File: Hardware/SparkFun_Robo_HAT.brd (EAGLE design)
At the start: 65.1 x 57 mm, 235 parts, among them J11 EXT MTR PWR, J18 ISP, J2 RASPBERRYPI-40-PIN-GPIO_SMD_S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, J20 USB C, J23 CORTEX_JTAG_DEBUG_PTH, J7 EXT SERVO PWR, J8 EXT 5V PWR, Q1 310mA/60V/1.6Ω, Q23 20V/0.2A/8MHz/1.2Ω/1Vth, Q24 20V/0.2A/8MHz/1.2Ω/1Vth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

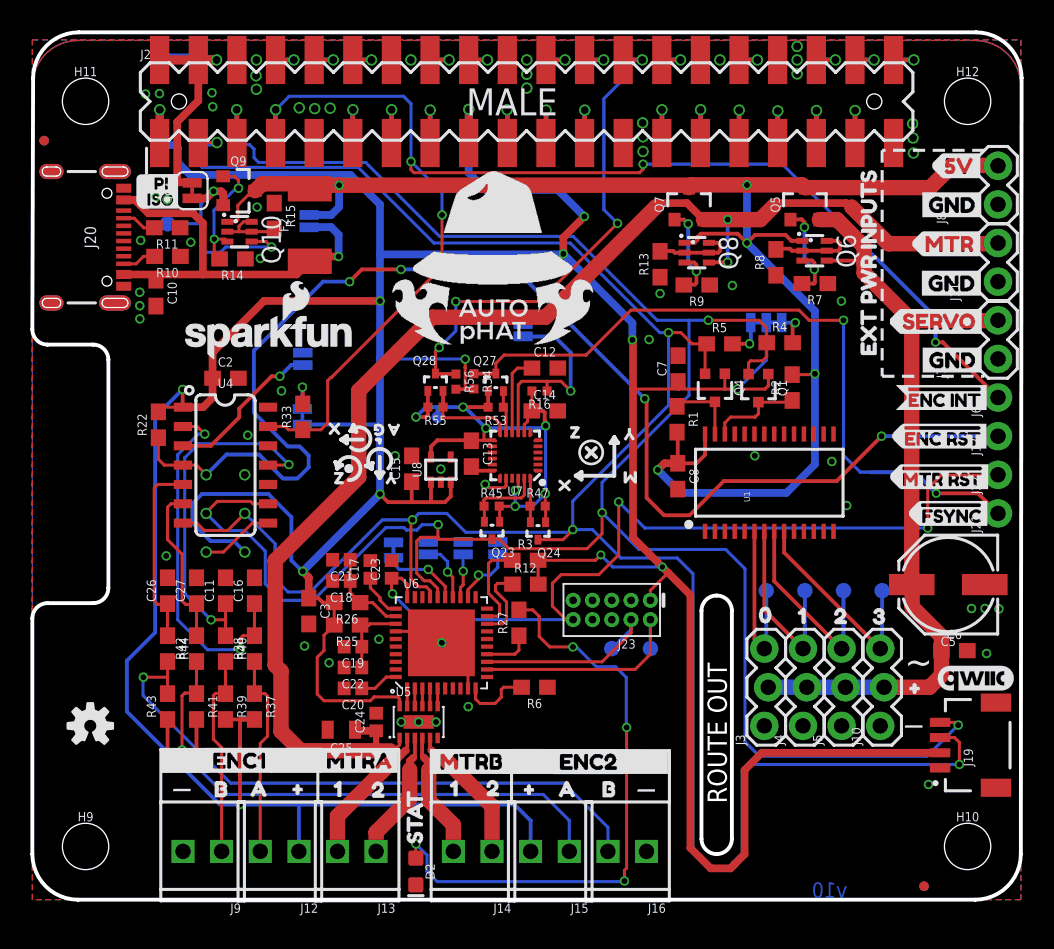
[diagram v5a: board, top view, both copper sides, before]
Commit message: Design review changes
-added more GND stiching VIAs to middle area of board (MTR VIN trace kind of cutts top GND pour in half diagnoly)
-rotated IMU axis labels to read same as other silk
-separated imu axis labels on bottom silk
-removed GND traces from Cypress thermal pad to GND pads
-added more gnd vias under cypress
-removed TP15 name text in SCH
-changes SCH to 9V MAX EXT MTR input, *11v MAX with heat sink)
-added "default" text to IMU address paragraph
-added test points for IMU INT and DC motors lines and encoder lines
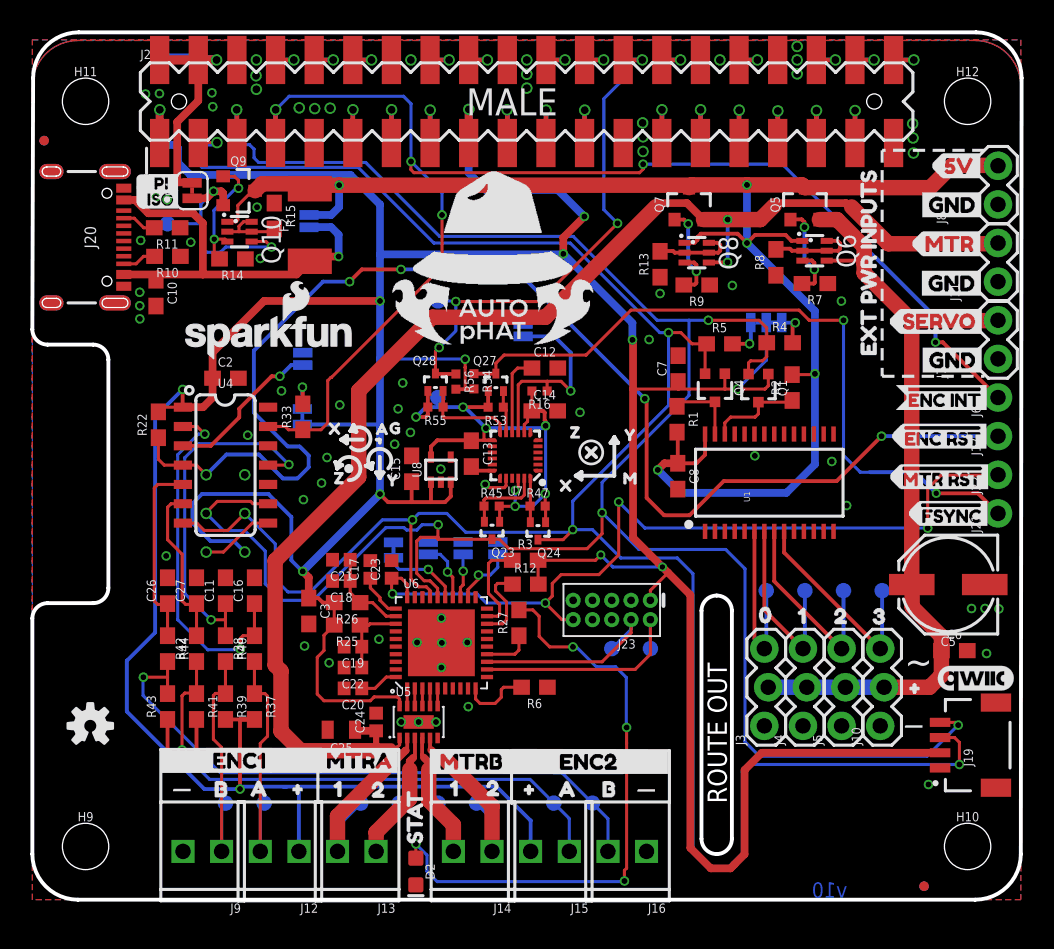
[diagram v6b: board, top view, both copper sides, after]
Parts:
- added TP10, TP11, TP12, TP13, TP14, TP15, TP16, TP17, TP18: (no value), SparkFun-Connectors:PAD.03X.04
- TP9: value (none) -> TEST-POINT3X4; device SparkFun-Connectors:PAD.03X.03 -> SparkFun-Connectors:PAD.03X.04
- moved U$130 4.17 mm to (34.5, 34.3), turned to 0 degrees
- moved U$127 3.14 mm to (34.4, 30.4), turned to 0 degrees
- moved U$107 2.99 mm to (21.9, 31.0), turned to 0 degrees
- moved U$129 2.33 mm to (33.7, 34.3), turned to 0 degrees
- moved U$108 2.33 mm to (38.1, 27.7), turned to 0 degrees
- moved U$110 2.05 mm to (38.2, 30.6), turned to 0 degrees
- moved U$104 2.00 mm to (22.6, 27.6), turned to 0 degrees
- moved U$109 1.56 mm to (36.1, 27.2), turned to 180 degrees
- moved U$123 1.52 mm to (22.0, 30.6)
- moved U$122 1.47 mm to (27.2, 30.7), turned to 0 degrees
- moved TP9 1.29 mm to (26.7, 33.0)
- moved U$126 1.23 mm to (31.3, 34.5)
- moved U$128 1.23 mm to (31.0, 30.7)
- moved U$124 1.14 mm to (27.6, 34.3), turned to 0 degrees
- moved U$125 1.13 mm to (24.2, 34.3), turned to 0 degrees
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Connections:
- net AOUT1: now also TP16.P$1
- net AOUT2: now also TP15.P$1
- net BOUT1: now also TP14.P$1
- net BOUT2: now also TP13.P$1
- net ENC1A_RAW: now also TP17.P$1
- net ENC1B_RAW: now also TP18.P$1
- net ENC2A_RAW: now also TP12.P$1
- net ENC2B_RAW: now also TP11.P$1
- net IMU_INT_3.3V: now also TP10.P$1
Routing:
- net AOUT1: track 9.46 -> 13.3 mm
- net AOUT2: track 8.59 -> 12.4 mm
- net BOUT2: track 9.33 -> 12.9 mm
- net BOUT1: track 8.32 -> 11.9 mm
- net GND: track 10.4 -> 6.85 mm, vias 60 -> 72
- net ENC1B_RAW: track 13.4 -> 16.7 mm
- net ENC1A_RAW: track 13.4 -> 16.7 mm
- net !MTR_RST: track 56.1 -> 54.4 mm, vias 3 -> 4
- net IMU_INT_3.3V: track 33.7 -> 35.0 mm
